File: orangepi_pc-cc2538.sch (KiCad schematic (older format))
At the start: 19 parts

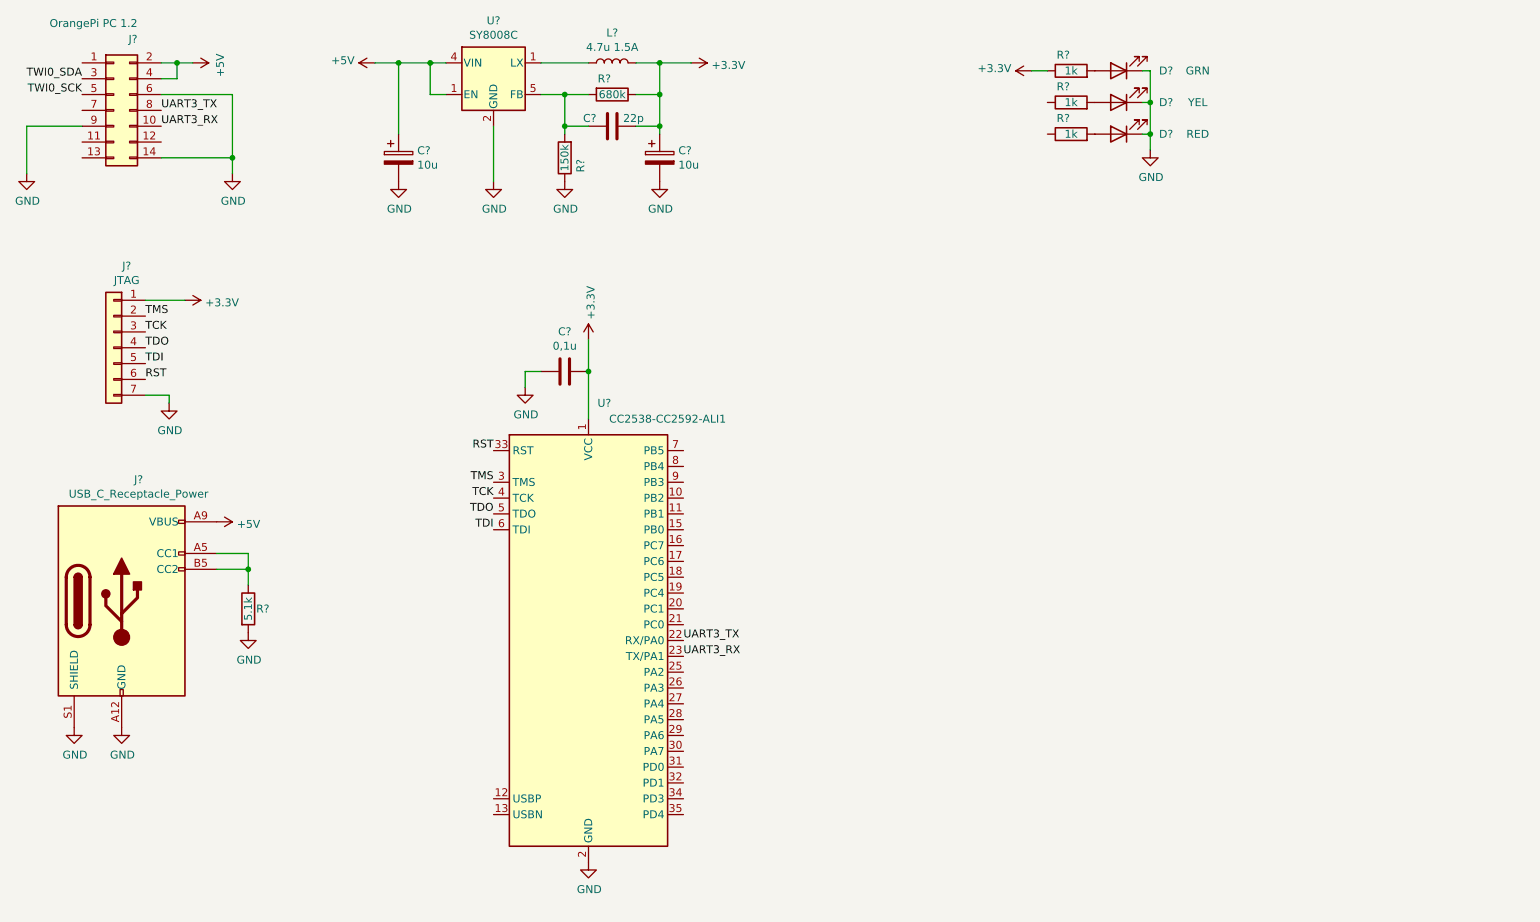
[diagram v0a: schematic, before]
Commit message: add RTC, LEDs, buttons to schematic
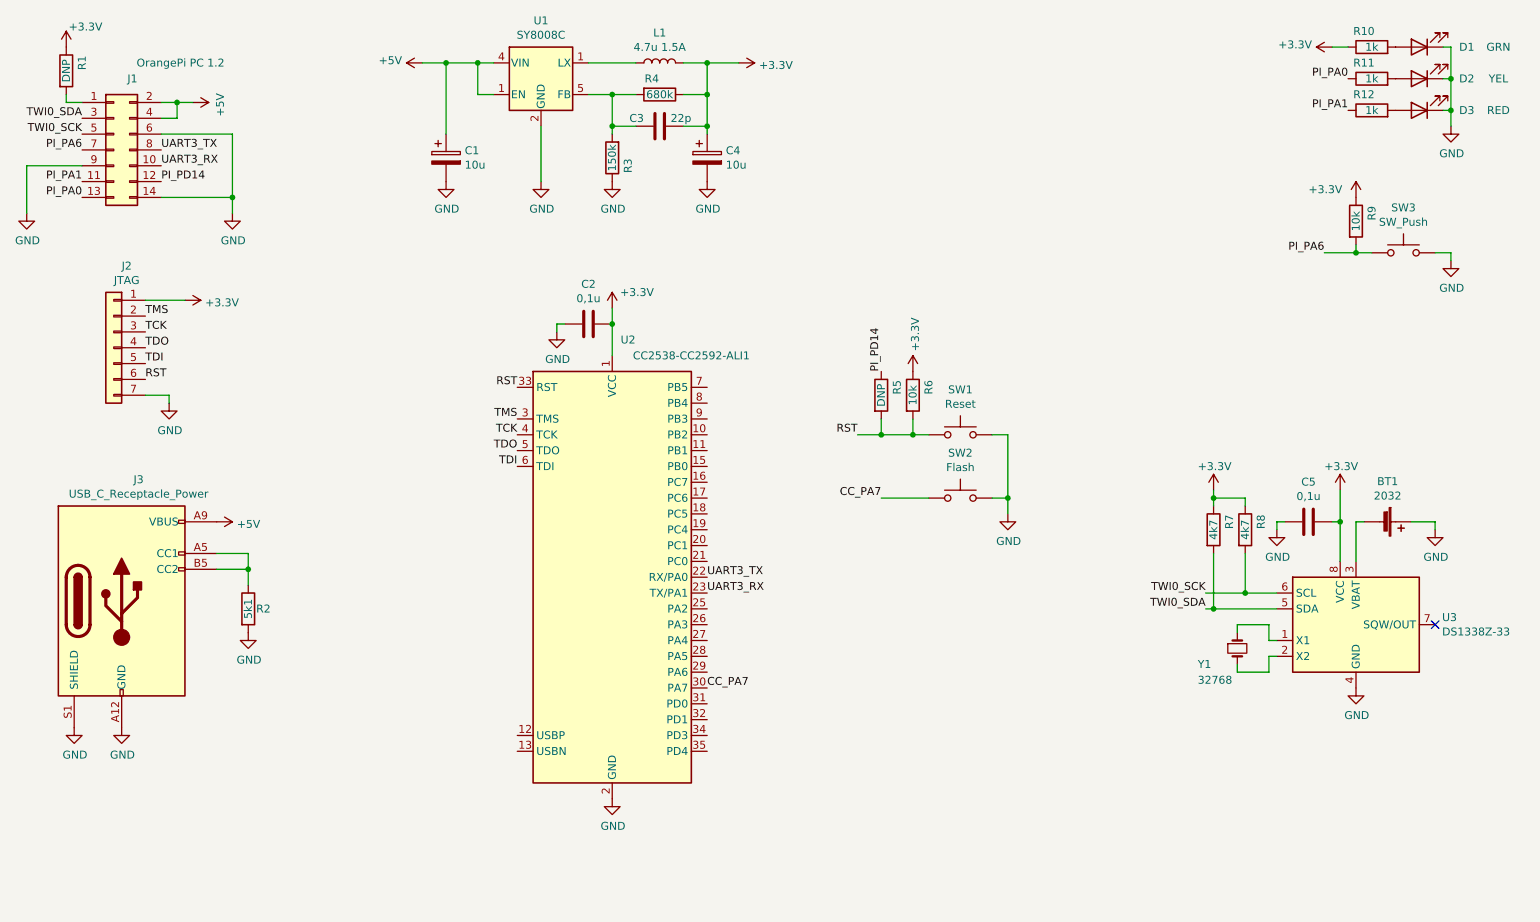
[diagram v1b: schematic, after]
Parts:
- added BT1: 2032, Battery:BatteryHolder_Keystone_3002_1x2032, symbol Device:Battery_Cell
- added C5: 0,1u, Capacitor_SMD:C_0603_1608Metric, symbol Device:C
- added R1, R5: DNP, Resistor_SMD:R_0603_1608Metric, symbol Device:R
- added R6, R9: 10k, Resistor_SMD:R_0603_1608Metric, symbol Device:R
- added R7, R8: 4k7, Resistor_SMD:R_0603_1608Metric, symbol Device:R
- added SW1: Reset, Button_Switch_SMD:SW_SPST_B3U-1000P, symbol Switch:SW_Push
- added SW2: Flash, Button_Switch_SMD:SW_SPST_B3U-1000P, symbol Switch:SW_Push
- added SW3: SW_Push, Button_Switch_THT:SW_Tactile_SPST_Angled_PTS645Vx39-2LFS, symbol Switch:SW_Push
- added U3: DS1338Z-33, Package_SO:SOIC-8_3.9x4.9mm_P1.27mm, symbol library:DS1338Z-33
- added Y1: 32768, Crystal:Crystal_SMD_SeikoEpson_MC406-4Pin_9.6x4.1mm, symbol Device:Crystal_Small
- C1, C4: renamed from C?; footprint (none) -> Capacitor_Tantalum_SMD:CP_EIA-3216-18_Kemet-A
- C2, C3: renamed from C?; footprint (none) -> Capacitor_SMD:C_0603_1608Metric
- D1, D2, D3: renamed from D?; footprint (none) -> LED_SMD:LED_0805_2012Metric
- J1: renamed from J?; footprint (none) -> Connector_PinSocket_2.54mm:PinSocket_2x07_P2.54mm_Vertical
- J2: renamed from J?; footprint (none) -> Connector_PinHeader_2.54mm:PinHeader_1x07_P2.54mm_Vertical
- J3: renamed from J?; footprint (none) -> Connector_USB:USB_C_Receptacle_HRO_TYPE-C-31-M-12
- L1: renamed from L?; footprint (none) -> Inductor_SMD:L_6.3x6.3_H3
- R10, R11, R12, R3, R4: renamed from R?; footprint (none) -> Resistor_SMD:R_0603_1608Metric
- R2: renamed from R?; value 5.1k -> 5k1; footprint (none) -> Resistor_SMD:R_0603_1608Metric
- gave numbers to parts that had none: 2
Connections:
- net +3V3: now also C5.1, R1.1, R6.1, R7.1, R8.1, R9.1, U3.8 (VCC)
- net GND: now also BT1.1 (+), C5.2, SW1.2, SW2.2, SW3.2, U3.4 (GND)
- net RST: now also R5.2, R6.2, SW1.1
- net TWI0_SCK: now also R8.2, U3.6 (SCL)
- net TWI0_SDA: now also R7.2, U3.5 (SDA)
- net CC_PA7: now reaches U2.30 (PA7)
- net CC_PA7: now also SW2.1
- net at J1.1 (Pin_1): now also R1.2
- net PI_PA1: now reaches J1.11 (Pin_11)
- net PI_PA1: now also R12.1
- net PI_PD14: now reaches J1.12 (Pin_12)
- net PI_PD14: now also R5.1
- net PI_PA0: now reaches J1.13 (Pin_13)
- net PI_PA0: now also R11.1
- net PI_PA6: now reaches J1.7 (Pin_7)
- net PI_PA6: now also R9.2, SW3.1
- new net: U3.1 (X1), Y1.1
- new net: U3.2 (X2), Y1.2
- new net: BT1.2 (-), U3.3 (VBAT)
- no-connect marks 0 -> 1
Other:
- moved on the sheet: C1, C2, C3, C4, D1, D2, D3, J1, L1, R10, R11, R12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

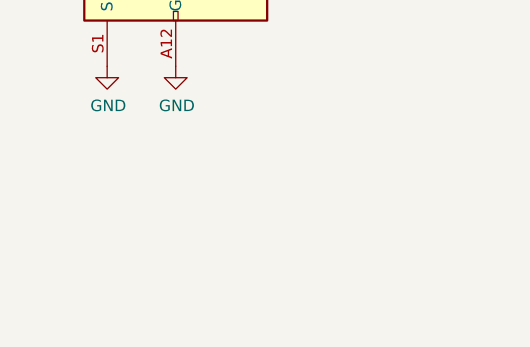
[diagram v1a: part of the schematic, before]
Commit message: add board outline
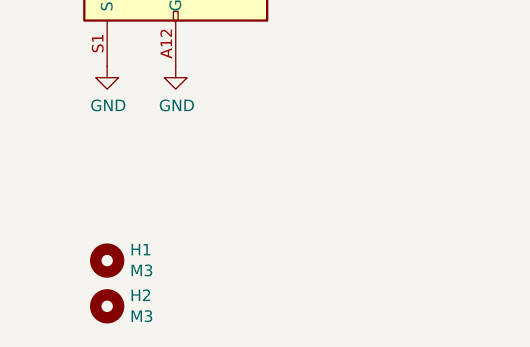
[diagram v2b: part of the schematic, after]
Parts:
- added H1, H2: M3, MountingHole:MountingHole_3.2mm_M3, symbol Mechanical:MountingHole
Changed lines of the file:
@@
 Wire Wire Line
 	1350 1300 1350 1250
+$Comp
+L Mechanical:MountingHole H1
+U 1 1 5F1DE0A8
+P 1400 6100
+F 0 "H1" H 1500 6146 50  0000 L CNN
+F 1 "M3" H 1500 6055 50  0000 L CNN
+F 2 "MountingHole:MountingHole_3.2mm_M3" H 1400 6100 50  0001 C CNN
+F 3 "~" H 1400 6100 50  0001 C CNN
+	1    1400 6100
+	1    0    0    -1
+$EndComp
+$Comp
+L Mechanical:MountingHole H2
+U 1 1 5F1DEC50
+P 1400 6300
+F 0 "H2" H 1500 6346 50  0000 L CNN
+F 1 "M3" H 1500 6255 50  0000 L CNN
+F 2 "MountingHole:MountingHole_3.2mm_M3" H 1400 6300 50  0001 C CNN
+F 3 "~" H 1400 6300 50  0001 C CNN
+	1    1400 6300
+	1    0    0    -1
+$EndComp
 $EndSCHEMATC
